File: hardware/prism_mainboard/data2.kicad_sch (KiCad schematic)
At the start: 2 parts, among them IC3 USB3320C-EZK, J1 503398-1892

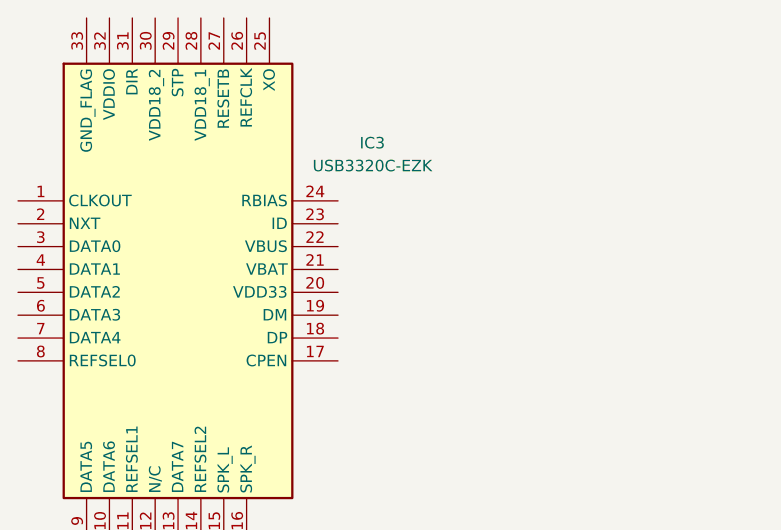
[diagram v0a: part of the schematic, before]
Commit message: Schematic Updates
Updated schematics. Most of the power and decoupling is set for most if not all devices. Need to interconnect devices. Still reading datasheets
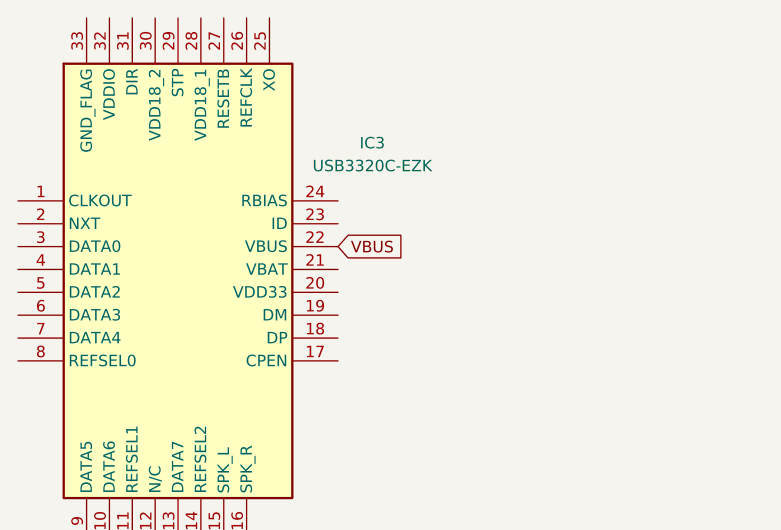
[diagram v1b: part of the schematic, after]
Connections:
- net VBUS: now reaches IC3.22 (VBUS)
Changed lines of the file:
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@@
 	(generator_version "10.0")
 	(paper "A4")
+	(global_label "VBUS"
+		(shape input)
+		(at 102.87 74.93 0)
+		(fields_autoplaced yes)
+		(effects
+			(font
+				(size 1.27 1.27)
+			)
+			(justify left)
+		)
+		(property "Intersheetrefs" "${INTERSHEET_REFS}"
+			(at 110.7538 74.93 0)
+			(hide yes)
+			(show_name no)
+			(do_not_autoplace no)
+			(effects
+				(font
+					(size 1.27 1.27)
+				)
+				(justify left)
+			)
+		)
+	)
 	(symbol
 		(lib_id "SamacSys:USB3320C-EZK")

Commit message: Updates
Mostly Schematic updates, nothing too big. Added a few datasheets
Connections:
- net CLKOUT: now reaches IC3.1 (CLKOUT)
- net USB_D6: now reaches IC3.10 (DATA6)
- net USB_D7: now reaches IC3.13 (DATA7)
- net DATA+: now reaches IC3.18 (DP)
- net DATA-: now reaches IC3.19 (DM)
- net NXT: now reaches IC3.2 (NXT)
- net RST_B: now reaches IC3.27 (RESETB)
- net STP: now reaches IC3.29 (STP)
- net USB_D0: now reaches IC3.3 (DATA0)
- net DIR: now reaches IC3.31 (DIR)
- net USB_D1: now reaches IC3.4 (DATA1)
- net USB_D2: now reaches IC3.5 (DATA2)
- net USB_D3: now reaches IC3.6 (DATA3)
- net USB_D4: now reaches IC3.7 (DATA4)
- net USB_D5: now reaches IC3.9 (DATA5)
- net SD_D2: now reaches J1.1 (DAT2)
- net SD_SWITCH: now reaches J1.10 (DETECT_SWITCH)
- net SD_D3: now reaches J1.2 (CD/DAT3)
- net SD_CMD: now reaches J1.3 (CMD)
- net +3.3V: now reaches J1.4 (VDD)
- net SD_CLK: now reaches J1.5 (CLK)
- net GND: now reaches J1.6 (VSS)
- net SD_D0: now reaches J1.7 (DAT0)
- net SD_D1: now reaches J1.8 (DAT1)
- net SD_LEVER: now reaches J1.9 (DETECT_LEVER)
